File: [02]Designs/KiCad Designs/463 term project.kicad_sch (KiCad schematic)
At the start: 73 parts, among them J4 Conn_01x03_Pin, Q1 BC547, Q10 PJMH099N60EC, Q2 BC547, Q7 PJMH099N60EC, Q8 PJMH099N60EC, Q9 PJMH099N60EC, U1 6N135, U2 6N135, U3 74HC00, U4 IR2110, U5 IR2110, U6 ACS712xLCTR-30A, U8 ADuM1200AR, U9 ADuM1200AR

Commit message: Schematic Updates: Added Brake Part
auxlary power design added

Co-Authored-By: KaanDemirkoparan <57269134+KaanDemirkoparan@users.noreply.github.com>
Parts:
- added Brake_Resistor1: 5, symbol Device:R
- added C23, C24, C27: 100n, symbol Device:C
- added C25, C28: 100u, symbol Device:C
- added C26: 20u, symbol Device:C
- added D19, D20: UF4007, Diode_THT:D_DO-41_SOD81_P10.16mm_Horizontal, symbol Diode:1N4001
- added J2, J3: Screw_Terminal_01x01, METUPowerLab_Boards_ESP32:Untitled, symbol Connector:Screw_Terminal_01x01
- added Q11: PJMH099N60EC, Package_TO_SOT_THT:TO-247-3_Vertical, symbol Transistor_FET:IRFP4468PbF
- added R14: 10, symbol Device:R
- added R15: 1k, symbol Device:R
- added U10: ADuM1200AR, Package_SO:SOIC-8_3.9x4.9mm_P1.27mm, symbol Isolator:ADuM1200AR
- added U11: IR2110, Package_DIP:DIP-14_W7.62mm, symbol Driver_FET:IR2110
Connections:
- net +12V: now also C24.1, C25.1, D19.2 (A), U11.3 (VCC)
- net +3.3V: now also U10.1 (VDD1)
- net +5V: now also C27.1, C28.1, U10.8 (VDD2), U11.9 (VDD)
- net GND: now also C27.2, C28.2, U10.5 (GND2), U11.11 (SD), U11.13 (VSS)
- net GNDA: now also C24.2, C25.2, Q11.3 (S), R15.1, U11.2 (COM)
- net GNDD: now also U10.4 (GND1)
- net Q7_Drain: now reaches C8.2, C9.2, D12.1 (K), D7.2 (A), Q7.2 (D), Q8.3 (S), R8.1, U4.5 (VS)
- net Q7_Drain: now also Brake_Resistor1.1, J2.1 (Pin_1)
- new net: D20.1 (K), R14.1, U11.1 (LO)
- new net: C23.2, C26.2, U11.5 (VS)
- new net: C23.1, C26.1, D19.1 (K), U11.6 (VB)
- new net: D20.2 (A), Q11.1 (G), R14.2, R15.2
- new net Q11_Drain: Brake_Resistor1.2, J3.1 (Pin_1), Q11.2 (D)
- new net S_brake_ISO: U10.7 (VOA), U11.12 (LIN)
- new net S_break: U10.2 (VIA)

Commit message: Schematic and Footprints are finished
Co-Authored-By: KaanDemirkoparan <57269134+KaanDemirkoparan@users.noreply.github.com>
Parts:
- added C29: 470u, Capacitor_THT:CP_Radial_D10.0mm_P2.50mm, symbol Device:C
- added C30, C31, C32, C36, C37, C39, C41: 100n, Capacitor_THT:C_Disc_D5.0mm_W2.5mm_P5.00mm, symbol Device:C
- added C33, C34, C35, C38, C40, C42: 22u, Capacitor_THT:CP_Radial_D8.0mm_P5.00mm, symbol Device:C
- added D1, D2: D, Diode_THT:D_DO-35_SOD27_P10.16mm_Horizontal, symbol Device:D
- added D9: *, KBPC3510FP:KBPC3510FP, symbol KBPC3510FP:Bridge_1ph
- added JP14, JP15: SolderJumper_2_Open, Jumper:SolderJumper-2_P1.3mm_Open_TrianglePad1.0x1.5mm, symbol Jumper:SolderJumper_2_Open
- added T1: Transformer_1P_2S, Transformer_THT:Transformer_Breve_TEZ-35x42, symbol Device:Transformer_1P_2S
- added U12, U13: LM7812_TO220, Package_TO_SOT_THT:TO-220-3_Vertical, symbol Regulator_Linear:LM7812_TO220
- added U14: LM7815_TO220, Package_TO_SOT_THT:TO-220-3_Vertical, symbol Regulator_Linear:LM7815_TO220
- added U15: LM78L05_SO8, Package_SO:SOIC-8_3.9x4.9mm_P1.27mm, symbol Regulator_Linear:LM78L05_SO8
- added U16, U17: LD1117S33TR_SOT223, Package_TO_SOT_SMD:SOT-223-3_TabPin2, symbol Regulator_Linear:LD1117S33TR_SOT223
- added U18: ~, our_library:5 button module, symbol our_library:5_Button
- C1, C10, C12, C15, C16, C18, C19, C23, C24, C27, C3, C5, C6, C8: footprint (none) -> Capacitor_THT:C_Disc_D5.0mm_W2.5mm_P5.00mm
- C11, C14, C17, C25, C28, C7: footprint (none) -> Capacitor_THT:CP_Radial_D8.0mm_P5.00mm
- C13, C26, C9: value 20u -> 22u; footprint (none) -> Capacitor_THT:CP_Radial_D8.0mm_P5.00mm
- C2, C4: footprint (none) -> Capacitor_THT:CP_Radial_D6.3mm_P2.50mm
- C20: value 100n -> 1n; footprint (none) -> METUPowerLab_Capacitors_Ceramics_SurfaceMounts:0603 Large
- C21: footprint (none) -> METUPowerLab_Capacitors_Ceramics_SurfaceMounts:0603 Large
- C22: footprint (none) -> our_library:1500uF
- JP10, JP11, JP12, JP13, JP6, JP7, JP8, JP9: footprint (none) -> Jumper:SolderJumper-2_P1.3mm_Open_TrianglePad1.0x1.5mm
- R1, R10, R11, R12, R13, R14, R15, R2, R3, R4, R5, R6, R7, R8, R9: footprint (none) -> Resistor_THT:R_Axial_DIN0207_L6.3mm_D2.5mm_P10.16mm_Horizontal
- U3: footprint (none) -> Package_DIP:DIP-14_W7.62mm_Socket
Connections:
- net GNDA is gone; now on net GND: C10.2, C11.2, C14.2, C15.2, C18.2, C19.2, C22.1, C24.2, C25.2, D11.2 (A), D12.2 (A), Q10.3 (S), Q11.3 (S), Q7.3 (S), R12.1, R13.2, R15.1, R7.1, U11.2 (COM), U4.2 (COM), U5.2 (COM)
- net S_break is gone; now on net S_brake_ISO: U10.2 (VIA)
- net +12V: now also C34.1, U13.3 (VO)
- net +3.3V: now also C39.1, C40.1, U16.2 (VO); no longer U10.1 (VDD1), U7.1 (3V3), U8.1 (VDD1), U9.1 (VDD1)
- net +5V: now also C37.1, C38.1, U15.1 (OUT), U16.3 (VI); no longer C21.1, J4.1 (Pin_1), U6.8 (VCC)
- net DC_200V: now also D9.1 (+)
- net GND: now also C29.2, C30.2, C31.2, C32.2, C33.2, C34.2, C35.2, C36.2, C37.2, C38.2, C39.2, C40.2, D9.3 (-), T1.4 (SB), T1.5 (SC), U12.2 (GND), U13.2 (GND), U14.2 (GND), U15.2 (GND), U15.3 (GND), U15.6 (GND), U15.7 (GND), U16.1 (GND); no longer C20.2, C21.2, D6.1 (K), J4.3 (Pin_3), U6.5 (GND)
- net GNDD: now also C20.2, C21.2, D6.1 (K), J4.3 (Pin_3), U6.5 (GND), C41.2, C42.2, U17.1 (GND), U18.3 (GND)
- net S1: now also JP7.1 (A), JP9.2 (B), U4.10 (HIN), U9.7 (VOA); no longer JP10.2 (B), U9.2 (VIA)
- net S1_ISO: now also JP10.2 (B), JP11.2 (B), U9.2 (VIA); no longer JP7.1 (A), JP9.2 (B), U4.10 (HIN), U9.7 (VOA)
- net S2: now also JP8.1 (A), U5.10 (HIN), U8.7 (VOA); no longer JP11.2 (B), U8.2 (VIA)
- net S2_ISO: now also U8.2 (VIA); no longer JP8.1 (A), U5.10 (HIN), U8.7 (VOA)
- net S3: now also JP6.1 (A), JP8.2 (B), U4.12 (LIN), U9.6 (VOB); no longer JP12.2 (B), U9.3 (VIB)
- net S3_ISO: now also JP12.2 (B), JP13.2 (B), U9.3 (VIB); no longer JP6.1 (A), JP8.2 (B), U4.12 (LIN), U9.6 (VOB)
- net S4: now also JP9.1 (A), U5.12 (LIN), U8.6 (VOB); no longer JP13.2 (B), U8.3 (VIB)
- net S4_ISO: now also U8.3 (VIB); no longer JP9.1 (A), U5.12 (LIN), U8.6 (VOB)
- net S_brake_ISO: now also JP15.2 (B); no longer U10.7 (VOA), U11.12 (LIN)
- net at R3.2: now also U3.11; no longer U3.6
- net at JP7.2 (B), Q1.1 (C): now also U3.3; no longer U3.11
- net at U3.1, U3.2, U3.4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: now also R1.2, U1.6; no longer R2.2, U2.6
- net at U7.19 (5V): now also JP14.1 (A)
- net Button2: now reaches U7.27 (IO16)
- net Button2: now also U18.4 (S2)
- net Button3: now reaches U7.28 (IO17)
- net Button3: now also U18.5 (S3)
- net Button4: now reaches U7.30 (IO18)
- net Button4: now also U18.6 (S4)
- net Button5: now reaches U7.31 (IO19)
- net Button5: now also U18.7 (S5)
- net at U7.6 (IO35): now also JP15.1 (A)
- net at JP6.2 (B), Q2.1 (C): now also U3.8; no longer U3.3
- net at U3.10, U3.12, U3.13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: now also R2.2, U2.6; no longer R1.2, U1.6
- net at R4.1: now also U3.6; no longer U3.8
- net BUTTON renamed Button1
- net Button1: now also U18.2 (S1)
- new net: C29.1, C30.1, C31.1, C32.1, D1.1 (K), D2.1 (K), U12.1 (VI), U13.1 (VI), U14.1 (VI)
- new net: C33.1, C36.1, U12.3 (VO), U15.8 (IN)
- new net: D2.2 (A), T1.6 (SD)
- new net: D1.2 (A), T1.3 (SA)
- new net +15V: C35.1, U14.3 (VO)
- new net +3.3V_Isolated: C41.1, C42.1, U10.1 (VDD1), U17.2 (VO), U18.1 (Vcc), U7.1 (3V3), U8.1 (VDD1), U9.1 (VDD1)
- new net +5V_Isolated: C21.1, J4.1 (Pin_1), JP14.2 (B), U17.3 (VI), U6.8 (VCC)
- new net 220V_Line: D9.2 (Input_~), T1.1 (AA)
- new net 220V_Neutral: D9.4 (Input_~), T1.2 (AB)
- new net S_brake: U10.7 (VOA), U11.12 (LIN)
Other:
- moved on the sheet: Brake_Resistor1, C1, C10, C11, C12, C13, C14, C15, C16, C17, C18, C19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

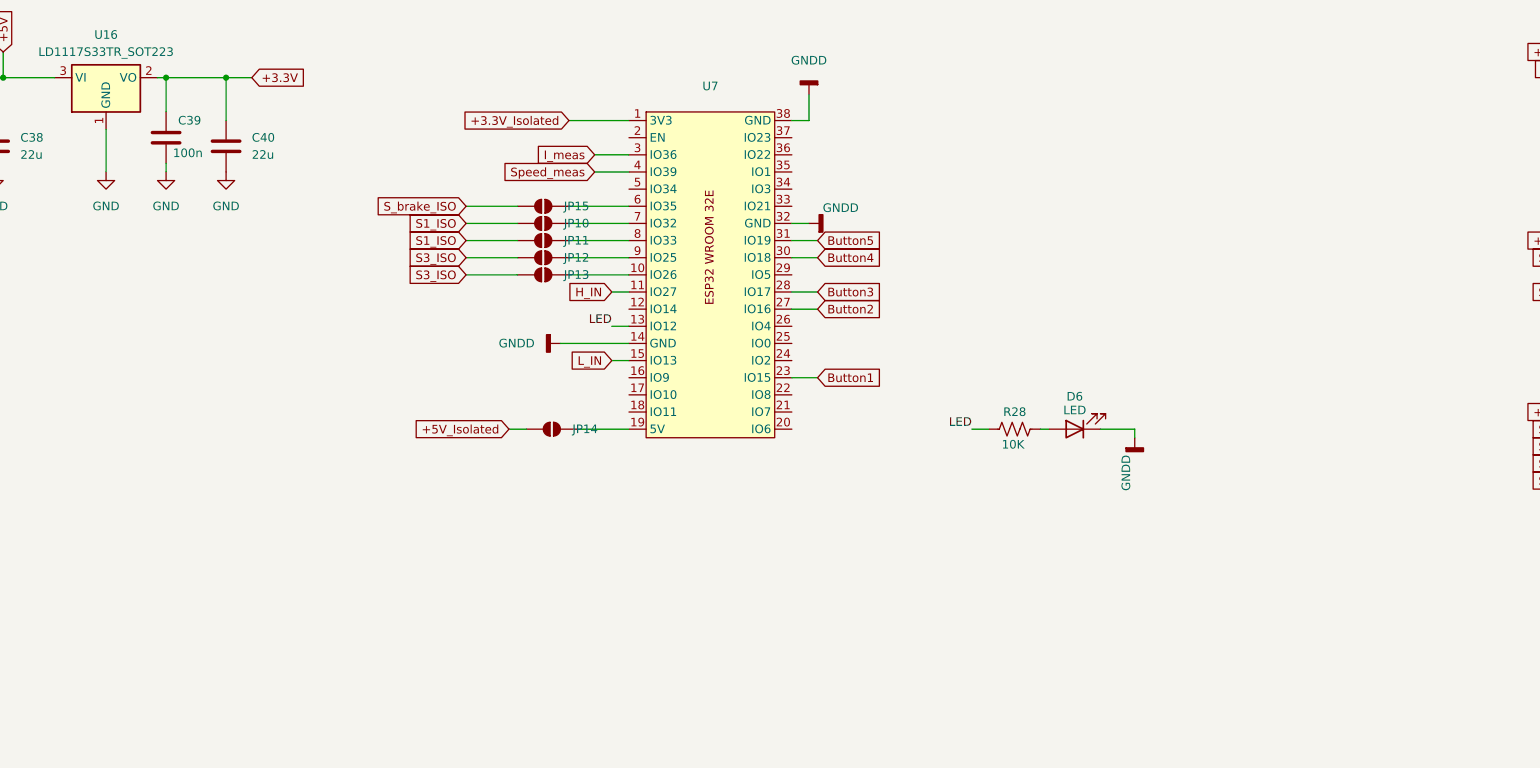
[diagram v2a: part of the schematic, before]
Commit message: schematic is updated
Co-Authored-By: KaanDemirkoparan <57269134+KaanDemirkoparan@users.noreply.github.com>
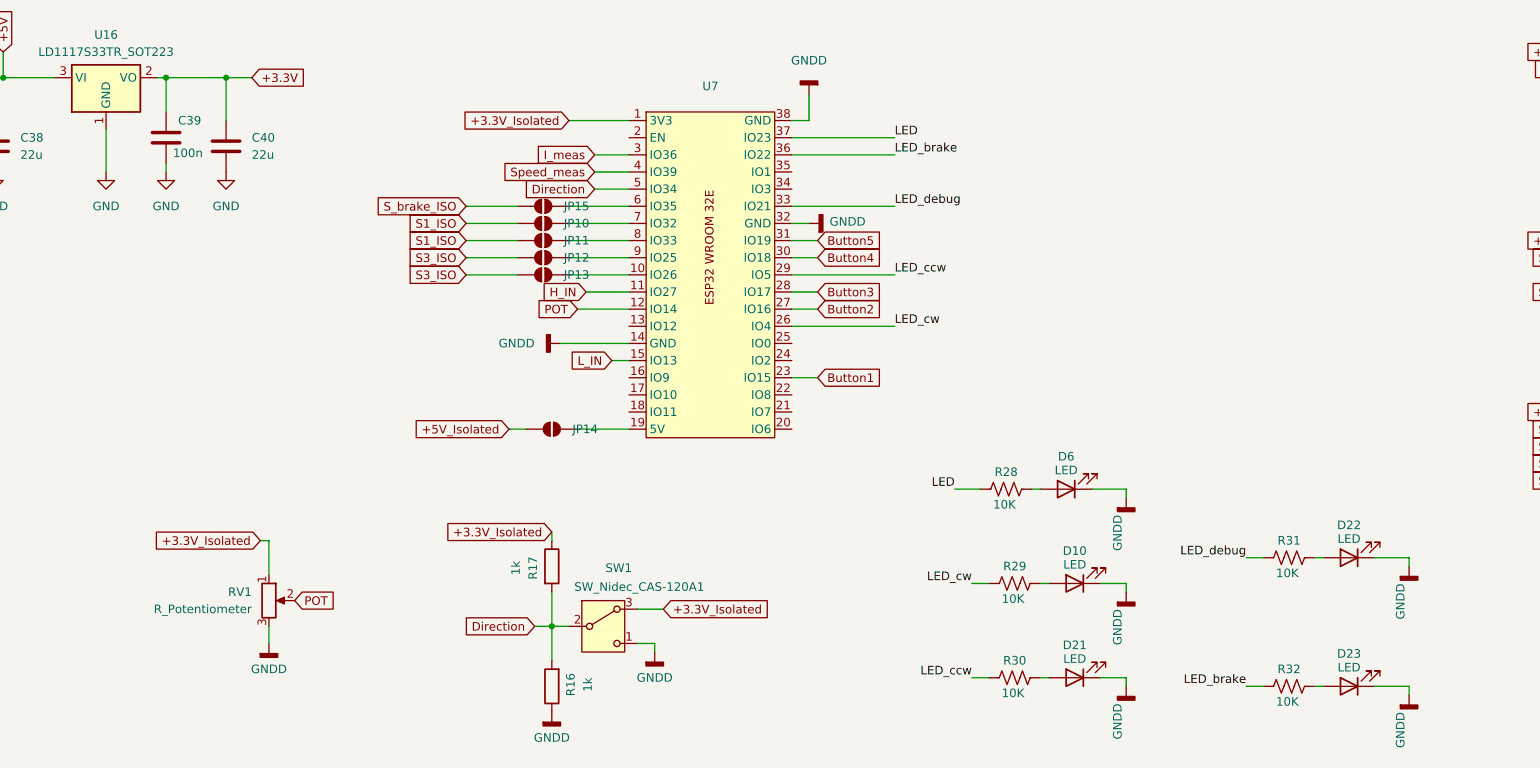
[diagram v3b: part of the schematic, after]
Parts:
- added D10, D21, D22, D23: LED, METUPowerLab_LEDs_SurfaceMounts:0603 Medium, symbol Device:LED
- added R16, R17: 1k, Resistor_THT:R_Axial_DIN0207_L6.3mm_D2.5mm_P10.16mm_Horizontal, symbol Device:R
- added R29, R30, R31, R32: 10K, METUPowerLab_Resistors_ChipResistors:0603 Medium, symbol Device:R_US
- added RV1: R_Potentiometer, Connector_PinHeader_2.54mm:PinHeader_1x03_P2.54mm_Vertical, symbol Device:R_Potentiometer
- added SW1: SW_Nidec_CAS-120A1, Connector_PinHeader_2.54mm:PinHeader_1x03_P2.54mm_Vertical, symbol Switch:SW_Nidec_CAS-120A1
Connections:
- net +3.3V_Isolated: now also R17.1, RV1.1, SW1.3 (A)
- net GNDD: now also D10.1 (K), D21.1 (K), D22.1 (K), D23.1 (K), R16.1, RV1.3, SW1.1 (C)
- net LED: now also U7.37 (IO23); no longer U7.13 (IO12)
- net POT: now reaches U7.12 (IO14)
- net POT: now also RV1.2
- net LED_cw: now reaches U7.26 (IO4)
- net LED_cw: now also R29.1
- net LED_ccw: now reaches U7.29 (IO5)
- net LED_ccw: now also R30.1
- net LED_debug: now reaches U7.33 (IO21)
- net LED_debug: now also R31.1
- net LED_brake: now reaches U7.36 (IO22)
- net LED_brake: now also R32.1
- net Direction: now reaches U7.5 (IO34)
- net Direction: now also R16.2, R17.2, SW1.2 (B)
- new net: D22.2 (A), R31.2
- new net: D21.2 (A), R30.2
- new net: D23.2 (A), R32.2
- new net: D10.2 (A), R29.2
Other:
- moved on the sheet: D6, R28

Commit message: Layout.v1 finished & Schematic updates
Co-Authored-By: KaanDemirkoparan <57269134+KaanDemirkoparan@users.noreply.github.com>
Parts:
- removed C5: 100n, Capacitor_THT:C_Disc_D5.0mm_W2.5mm_P5.00mm, symbol Device:C
- removed D1, D2: D, Diode_THT:D_DO-35_SOD27_P10.16mm_Horizontal, symbol Device:D
- removed T1: Transformer_1P_2S, Transformer_THT:Transformer_Breve_TEZ-35x42, symbol Device:Transformer_1P_2S
- removed U12, U13: LM7812_TO220, Package_TO_SOT_THT:TO-220-3_Vertical, symbol Regulator_Linear:LM7812_TO220
- removed U15: LM78L05_SO8, Package_SO:SOIC-8_3.9x4.9mm_P1.27mm, symbol Regulator_Linear:LM78L05_SO8
- added C43: 100n, Capacitor_THT:C_Disc_D5.0mm_W2.5mm_P5.00mm, symbol Device:C
- added D24, D5: 1N5408, Diode_THT:D_DO-201AD_P15.24mm_Horizontal, symbol Diode:1N5408
- added J5, J6: Screw_Terminal_01x01, METUPowerLab_Boards_ESP32:Untitled, symbol Connector:Screw_Terminal_01x01
- added T2: Transformer, Transformer_THT:Transformer_Breve_TEZ-35x42, symbol our_library:Transformer
- added U12: LM7805_TO220, Package_TO_SOT_THT:TO-220-3_Vertical, symbol Regulator_Linear:LM7805_TO220
- added U19, U20: LM7812_TO220, Package_TO_SOT_THT:TO-220-3_Vertical, symbol Regulator_Linear:LM7812_TO220
- U16, U17: footprint Package_TO_SOT_SMD:SOT-223-3_TabPin2 -> Package_TO_SOT_THT:TO-220-3_Vertical
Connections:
- net +12V: now also U20.3 (VO)
- net +3.3V_Isolated: now also C43.1
- net +5V: now also U12.3 (VO)
- net 220V_Line: now also T2.6 (AA)
- net 220V_Neutral: now also T2.10 (AB)
- net GND: now also T2.2 (SC), T2.4 (SB), U12.2 (GND), U19.2 (GND), U20.2 (GND)
- net GNDD: now also C43.2
- net Q7_Drain: now also J5.1 (Pin_1)
- net at C12.2, C13.2, D11.1 (K)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: now also J6.1 (Pin_1)
- net at C29.1, C30.1, C31.1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: now also D24.1 (K), D5.1 (K), U19.1 (VI), U20.1 (VI)
- net at C33.1, C36.1: now also U12.1 (VI), U19.3 (VO)
- new net: D5.2 (A), T2.5 (SA)
- new net: D24.2 (A), T2.1 (SD)

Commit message: Layout and schematic updates
Co-Authored-By: KaanDemirkoparan <57269134+KaanDemirkoparan@users.noreply.github.com>
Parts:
- removed JP6, JP7, JP8, JP9: SolderJumper_2_Open, Jumper:SolderJumper-2_P1.3mm_Open_TrianglePad1.0x1.5mm, symbol Jumper:SolderJumper_2_Open
- added J1, J18, J19, J20, J7: Conn_01x02_Pin, Connector_PinHeader_2.54mm:PinHeader_1x02_P2.54mm_Vertical, symbol Connector:Conn_01x02_Pin
- added J10, J11, J12, J13, J16, J17, J8, J9: Conn_01x01_Pin, Connector_Wire:SolderWirePad_1x01_SMD_5x10mm, symbol Connector:Conn_01x01_Pin
- added J14, J15: Conn_01x01_Pin, Connector_Wire:SolderWirePad_1x01_SMD_1x2mm, symbol Connector:Conn_01x01_Pin
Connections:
- net +3.3V_Isolated: now also J1.1 (Pin_1); no longer C41.1, C42.1, U17.2 (VO)
- net +5V_Isolated: now also J14.1 (Pin_1)
- net 220V_Line: now also J17.1 (Pin_1), J9.1 (Pin_1)
- net 220V_Neutral: now also J16.1 (Pin_1), J8.1 (Pin_1)
- net GNDD: now also J15.1 (Pin_1)
- net Q11_Drain: now also J13.1 (Pin_1)
- net S1: now also J18.1 (Pin_1), J20.2 (Pin_2)
- net S1_ISO: no longer JP11.2 (B)
- net S2: now also J7.2 (Pin_2)
- net S2_ISO: now also JP11.2 (B)
- net S3: now also J19.2 (Pin_2), J7.1 (Pin_1)
- net S3_ISO: no longer JP13.2 (B)
- net S4: now also J18.2 (Pin_2)
- net S4_ISO: now also JP13.2 (B)
- net Current_Sense_out: now reaches C18.1, C19.1, D7.1 (K), D8.1 (K), Q8.2 (D), Q9.2 (D), U6.3 (IP-), U6.4 (IP-)
- net S4_Drain: now reaches C12.2, C13.2, D11.1 (K), D8.2 (A), J6.1 (Pin_1), Q10.2 (D), Q9.3 (S), R11.1, U5.5 (VS)
- net S4_Drain: now also J11.1 (Pin_1)
- net at Q1.1 (C), U3.3: now also J20.1 (Pin_1)
- net at Q2.1 (C), U3.8: now also J19.1 (Pin_1)
- net Q7_Drain renamed S3_Drain
- net S3_Drain: now also J10.1 (Pin_1), J12.1 (Pin_1)
- new net: C41.1, C42.1, J1.2 (Pin_2), U17.2 (VO)

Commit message: [Design] Layout Finished
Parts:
- removed JP10, JP11, JP12, JP13, JP15: SolderJumper_2_Open, Jumper:SolderJumper-2_P1.3mm_Open_TrianglePad1.0x1.5mm, symbol Jumper:SolderJumper_2_Open
- added J21, J22, J23, J24, J25, J26: Conn_01x02_Pin, Connector_PinHeader_2.54mm:PinHeader_1x02_P2.54mm_Vertical, symbol Connector:Conn_01x02_Pin
- J4: footprint (none) -> Connector_PinHeader_2.54mm:PinHeader_1x03_P2.54mm_Vertical
- U18: value ~ -> 5 Button Module
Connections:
- net +5V_Isolated: now also J21.1 (Pin_1); no longer JP14.2 (B)
- net 220V_Line: now also D9.4 (Input_~); no longer D9.2 (Input_~)
- net 220V_Neutral: now also D9.2 (Input_~); no longer D9.4 (Input_~)
- net GND: no longer C10.2, C11.2, C14.2, C15.2, C18.2, C19.2, C22.1, C24.2, C25.2, D11.2 (A), D12.2 (A), D9.3 (-), Q10.3 (S), Q11.3 (S), Q7.3 (S), R12.1, R13.2, R15.1, R7.1, U11.2 (COM), U4.2 (COM), U5.2 (COM)
- net S1_ISO: now also J24.2 (Pin_2)
- net S2_ISO: now also J26.2 (Pin_2)
- net S3_ISO: now also J23.2 (Pin_2)
- net S4_ISO: now also J25.2 (Pin_2)
- net S_brake_ISO: now also J22.2 (Pin_2)
- net at U7.7 (IO32): now also J23.1 (Pin_1)
- net at U7.10 (IO26): now also J26.1 (Pin_1)
- net at U7.19 (5V): now also J21.2 (Pin_2); no longer JP14.1 (A)
- net at U7.6 (IO35): now also J22.1 (Pin_1)
- net at U7.8 (IO33): now also J24.1 (Pin_1)
- net at U7.9 (IO25): now also J25.1 (Pin_1)
- new net GNDPWR: C10.2, C11.2, C14.2, C15.2, C18.2, C19.2, C22.1, C24.2, C25.2, D11.2 (A), D12.2 (A), D9.3 (-), Q10.3 (S), Q11.3 (S), Q7.3 (S), R12.1, R13.2, R15.1, R7.1, U11.2 (COM), U4.2 (COM), U5.2 (COM)
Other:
- note added: "220 V Line & Neutral Solder Pads"
- note added: "5V Adapter"
- moved on the sheet: Brake_Resistor1, C22, C29, C30, C31, C32, C33, C34, C35, C36, C37, C38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
